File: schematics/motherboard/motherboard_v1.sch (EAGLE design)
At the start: 2 parts

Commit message: Motherboard reference design
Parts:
- added C1, C2: 2.2u (ESR<2R), SparkFun-Capacitors:CAP1206
- added C10: 1u, SparkFun-Capacitors:CAP1206
- added C11, C12, C13, C3, C4, C5, C6, C8, C9: 100n, SparkFun-Capacitors:CAP1206
- added C7: 10u, SparkFun-Capacitors:CAP1206
- added R1: 22R, SparkFun-Resistors:RESISTOR1206
- added R2, R3, R4, R5: 10k, SparkFun-Resistors:RESISTOR1206
- added S1: FSM4JSMA, meca:TAC_SWITCH
- added SW1: A6H2101, SparkFun-Electromechanical:SW_DIP-2-SMT-HALFSIZE
- added Y1: 25MHz, SparkFun-FreqCtrl:CRYSTALSMD
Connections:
- removed net TCK: JP1.TCK
- removed net TDI: JP1.TDI
- removed net TDO: JP1.TDO
- removed net TMS: JP1.TMS
- new net BOOT0: R4.1, U$1.BOOT0
- new net BOOT1: R5.1, U$1.PB2/BOOT1
- new net JNTRST: JP1.NTRST, U$1.PB4/NJTRST
- new net JTCK: JP1.TCK, U$1.PA14/JTCK/SWCLK
- new net JTDI: JP1.TDI, U$1.PA15/JTDI
- new net JTDO: JP1.TDO, U$1.PB3/JTDO/TRACESWO
- new net JTMS: JP1.TMS, U$1.PA13/JTMS/SWDIO
- new net N$1: C1.1, U$1.VCAP_1
- new net N$2: C2.1, U$1.VCAP_2
- new net N$3: C12.1, U$1.PH1/OSCOUT, Y1.1
- new net N$4: JP1.NSRRST, R1.1
- new net N$5: C13.1, U$1.PH0/OSCIN, Y1.2
- new net N$6: R3.2, R4.2, SW1.1
- new net N$7: R2.2, R5.2, SW1.2
- new net NRST: C11.1, R1.2, S1.3, S1.4, U$1.NRST
- net 3.3V: now also C10.1, C3.1, C4.1, C5.1, C6.1, C7.1, C8.1, C9.1, SW1.3, SW1.4
- net GND: now also C1.2, C10.2, C11.2, C12.2, C13.2, C2.2, C3.2, C4.2, C5.2, C6.2, C7.2, C8.2, C9.2, R2.1, R3.1, S1.1, S1.2
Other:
- note added: "Boot selection: 1 2 | Mode OFF --- | Flash ON OFF | Bootloader ON ON | SRAM"
- note added: "Decoupling each VDD + global"
- moved on the sheet: U$1

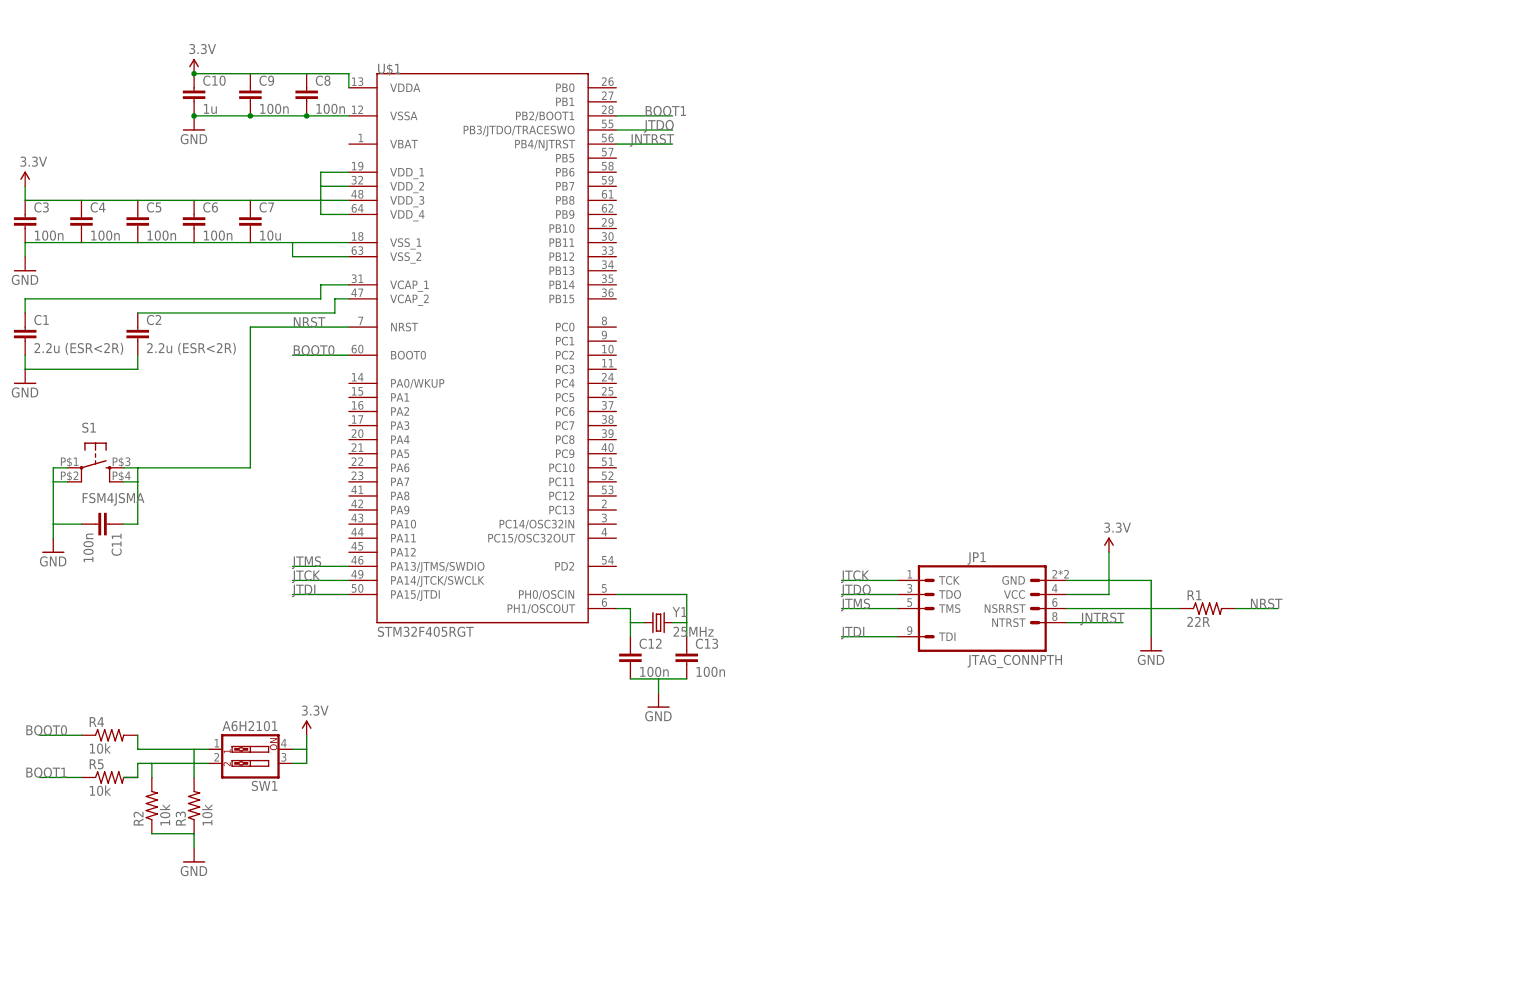
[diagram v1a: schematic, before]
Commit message: Library refactor and motherboard update
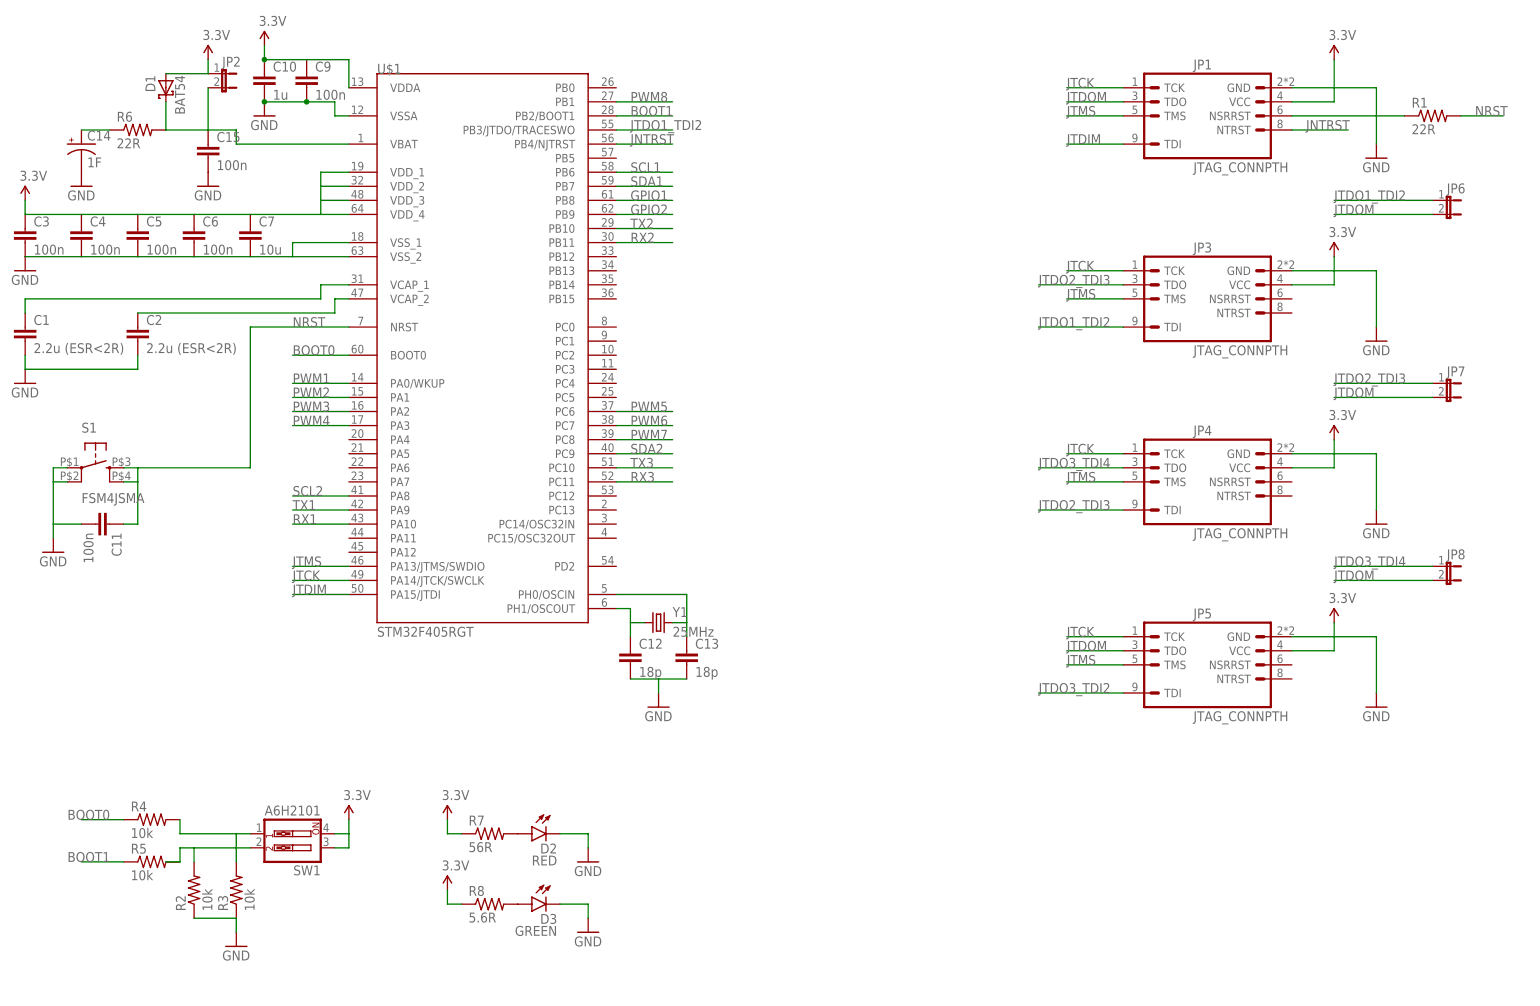
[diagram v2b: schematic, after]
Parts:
- removed C8: 100n, SparkFun-Capacitors:CAP1206
- added C14: 1F, Skippy-Passive:SUPERCAP
- added C15: 100n, SparkFun-Capacitors:CAP1206
- added D1: BAT54, diode:BAT54
- added D2: RED, SparkFun-LED:LED1206
- added D3: GREEN, SparkFun-LED:LED1206
- added JP2, JP6, JP7, JP8: (no value), SparkFun-Retired:JUMPER-2SMD-NO
- added JP3, JP4, JP5: JTAG_CONNPTH, connectors:JTAG_CONNPTH
- added R6: 22R, SparkFun-Resistors:RESISTOR1206
- added R7: 56R, SparkFun-Resistors:RESISTOR1206
- added R8: 5.6R, SparkFun-Resistors:RESISTOR1206
- C12, C13: value 100n -> 18p
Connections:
- net JTDI renamed JTDIM
- removed net JTDO: JP1.TDO, U$1.PB3/JTDO/TRACESWO
- new net GPIO1: U$1.PB8
- new net GPIO2: U$1.PB9
- new net JTDO1_TDI2: JP3.TDI, JP6.1, U$1.PB3/JTDO/TRACESWO
- new net JTDO2_TDI3: JP3.TDO, JP4.TDI, JP7.1
- new net JTDO3_TDI2: JP5.TDI
- new net JTDO3_TDI4: JP4.TDO, JP8.1
- new net JTDOM: JP1.TDO, JP5.TDO, JP6.2, JP7.2, JP8.2
- new net N$10: C15.1, D1.C, JP2.2, R6.2, U$1.VBAT
- new net N$11: D3.A, R8.2
- new net N$8: D2.A, R7.2
- new net N$9: C14.+, R6.1
- new net PWM1: U$1.PA0/WKUP
- new net PWM2: U$1.PA1
- new net PWM3: U$1.PA2
- new net PWM4: U$1.PA3
- new net PWM5: U$1.PC6
- new net PWM6: U$1.PC7
- new net PWM7: U$1.PC8
- new net PWM8: U$1.PB1
- new net RX1: U$1.PA10
- new net RX2: U$1.PB11
- new net RX3: U$1.PC11
- new net SCL1: U$1.PB6
- new net SCL2: U$1.PA8
- new net SDA1: U$1.PB7
- new net SDA2: U$1.PC9
- new net TX1: U$1.PA9
- new net TX2: U$1.PB10
- new net TX3: U$1.PC10
- net 3.3V: now also D1.A, JP2.1, JP3.VCC, JP4.VCC, JP5.VCC, R7.1, R8.1; no longer C8.1
- net GND: now also C14.-, C15.2, D2.C, D3.C, JP3.GND, JP4.GND, JP5.GND; no longer C8.2
- net JTCK: now also JP3.TCK, JP4.TCK, JP5.TCK
- net JTMS: now also JP3.TMS, JP4.TMS, JP5.TMS
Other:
- note added: "No fit w/o supercap"
- moved on the sheet: C10, C3, C4, C5, C6, C7, C9, JP1, R1, R2, R3, R4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

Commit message: Bluetooth debug module and external boards lib. Motherboard update
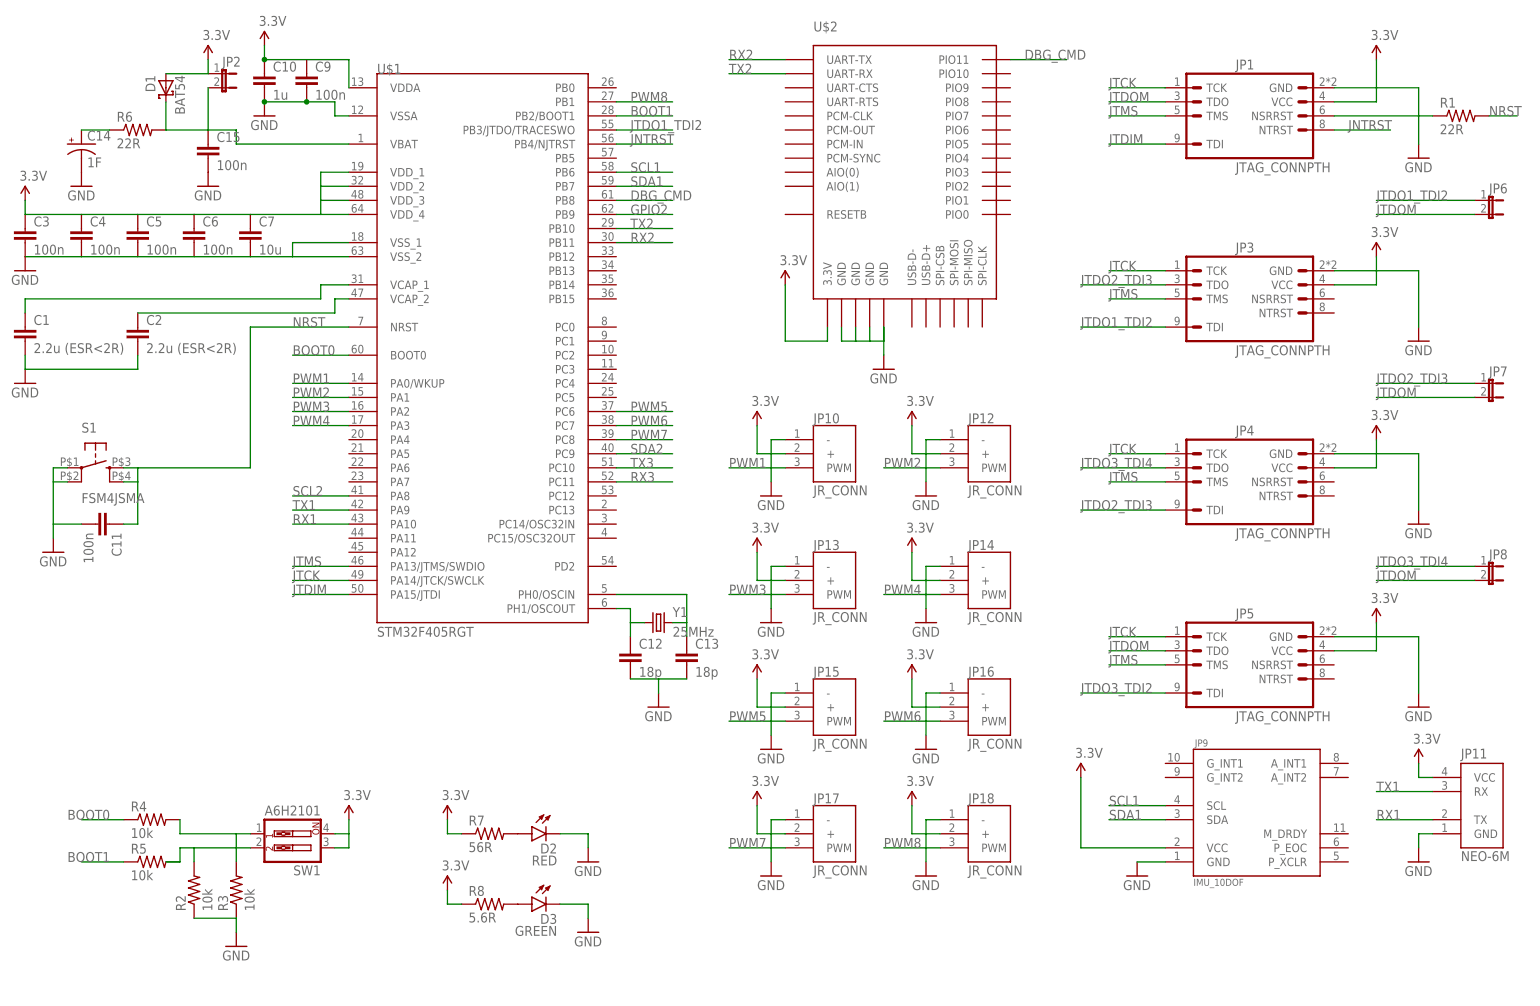
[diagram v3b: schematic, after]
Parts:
- added JP10, JP12, JP13, JP14, JP15, JP16, JP17, JP18: JR_CONN, Skippy-Connectors:JR_CONN
- added JP11: NEO-6M, Skippy-ExtBoards:NEO-6M
- added JP9: IMU_10DOF, Skippy-ExtBoards:IMU_10DOF
- added U$2: (no value), Skippy-ExtBoards:BTM400_6B
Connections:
- removed net GPIO1: U$1.PB8
- new net DBG_CMD: U$1.PB8, U$2.PIO11
- net 3.3V: now also JP10.+, JP11.VCC, JP12.+, JP13.+, JP14.+, JP15.+, JP16.+, JP17.+, JP18.+, JP9.VCC, U$2.3.3V
- net GND: now also JP10.-, JP11.GND, JP12.-, JP13.-, JP14.-, JP15.-, JP16.-, JP17.-, JP18.-, JP9.GND, U$2.GND@1, U$2.GND@2, U$2.GND@3, U$2.GND@4
- net PWM1: now also JP10.PWM
- net PWM2: now also JP12.PWM
- net PWM3: now also JP13.PWM
- net PWM4: now also JP14.PWM
- net PWM5: now also JP15.PWM
- net PWM6: now also JP16.PWM
- net PWM7: now also JP17.PWM
- net PWM8: now also JP18.PWM
- net RX1: now also JP11.TX
- net RX2: now also U$2.UART-TX
- net SCL1: now also JP9.SCL
- net SDA1: now also JP9.SDA
- net TX1: now also JP11.RX
- net TX2: now also U$2.UART-RX
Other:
- moved on the sheet: JP1, JP3, JP4, JP5, JP6, JP7, JP8, R1

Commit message: Motherboard update and PCB draft
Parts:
- added C16: 10u, SparkFun-Capacitors:CAP1206
- added C8: 100n, SparkFun-Capacitors:CAP1206
- added D4: ORANGE, SparkFun-LED:LED1206
- added IC1: 3.3V, SparkFun-PowerIC:V_REG_LM1117SOT223
- added JP19, JP20, JP21, JP22: M02PTH, SparkFun-Connectors:M02PTH
- added JP23: (no value), SparkFun-Retired:JUMPER-2SMD-NO
- added JP24: (no value), SparkFun-Connectors:M05PTH
- added JP25: JUMPER-31-2, SparkFun-Retired:JUMPER-31-2
- added R10: 1K8, SparkFun-Resistors:RESISTOR1206
- added R11: 3K3, SparkFun-Resistors:RESISTOR1206
- added R12, R13, R14, R15: 4K7, SparkFun-Resistors:RESISTOR1206
- added R9: 56R, SparkFun-Resistors:RESISTOR1206
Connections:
- removed net GPIO2: U$1.PB9
- new net LED1: R8.1, U$1.PB12
- new net LED2: R9.1, U$1.PB13
- new net N$12: JP24.2, R10.2, R11.2
- new net N$13: JP24.1, JP25.2
- new net N$15: D4.A, R9.2
- new net VDD: C8.1, IC1.IN, JP19.1, JP23.1, JP24.4, JP25.1
- net 3.3V: now also C16.1, IC1.OUT, JP23.2, R12.2, R13.2, R14.2, R15.2; no longer R8.1
- net GND: now also C16.2, C8.2, D4.C, IC1.ADJ, JP19.2, JP24.5, JP25.3, R11.1; no longer U$2.GND@2, U$2.GND@3
- net RX3: now also R10.1
- net SCL1: now also JP22.2, R13.1
- net SCL2: now also JP20.2, JP21.2, R14.1
- net SDA1: now also JP22.1, R12.1
- net SDA2: now also JP20.1, JP21.1, R15.1
- net TX3: now also JP24.3
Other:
- note added: "Telemetry"
- moved on the sheet: C11, D2, D3, JP1, JP3, JP4, JP5, JP6, JP7, JP8, R1, R2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

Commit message: MB PCB update
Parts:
- removed JP5: JTAG_CONNPTH, connectors:JTAG_CONNPTH
- removed JP8: (no value), SparkFun-Retired:JUMPER-2SMD-NO
- removed U$2: (no value), Skippy-ExtBoards:BTM400_6B
- added JP26, JP27: (no value), SparkFun-Connectors:M05PTH
- C15, C3, C4, C5, C6, C9: device SparkFun-Capacitors:CAP1206 -> SparkFun-Capacitors:CAP0805
- JP11: value NEO-6M -> (none); device Skippy-ExtBoards:NEO-6M -> SparkFun-Connectors:M05PTH
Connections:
- removed net JTDO3_TDI2: JP5.TDI
- removed net JTDO3_TDI4: JP4.TDO, JP8.1
- new net US_ECHO: JP11.3, U$1.PB15
- new net US_TRIGGER: JP11.4, U$1.PB14
- net 3.3V: now also JP26.4, JP27.4; no longer JP11.VCC, JP5.VCC, U$2.3.3V
- net DBG_CMD: now also JP26.1; no longer U$2.PIO11
- net GND: now also JP11.1, JP26.5, JP27.5; no longer JP11.GND, JP5.GND, U$2.GND@1, U$2.GND@4
- net JTCK: no longer JP5.TCK
- net JTDOM: now also JP4.TDO; no longer JP5.TDO, JP8.2
- net JTMS: no longer JP5.TMS
- net RX1: now also JP27.2; no longer JP11.TX
- net RX2: now also JP26.2; no longer U$2.UART-TX
- net TX1: now also JP27.3; no longer JP11.RX
- net TX2: now also JP26.3; no longer U$2.UART-RX
- net VDD: now also JP11.5
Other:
- note added: "10DOF IMU"
- note added: "Debug"
- note added: "GPS"
- note added: "IIC buses"
- note added: "SRF-04"
- moved on the sheet: JP10, JP12, JP13, JP14, JP15, JP16, JP17, JP18, JP20, JP21, JP22, JP9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
